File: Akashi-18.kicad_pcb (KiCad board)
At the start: 2 copper layers, 54.6 x 91.4 mm, 13 parts, among them Q1 DTC143Z, Q2 DTC143Z, Q3 DTC143Z, SW1 B3FS, SW2 B3FS, SW3 B3FS, U1 Pico

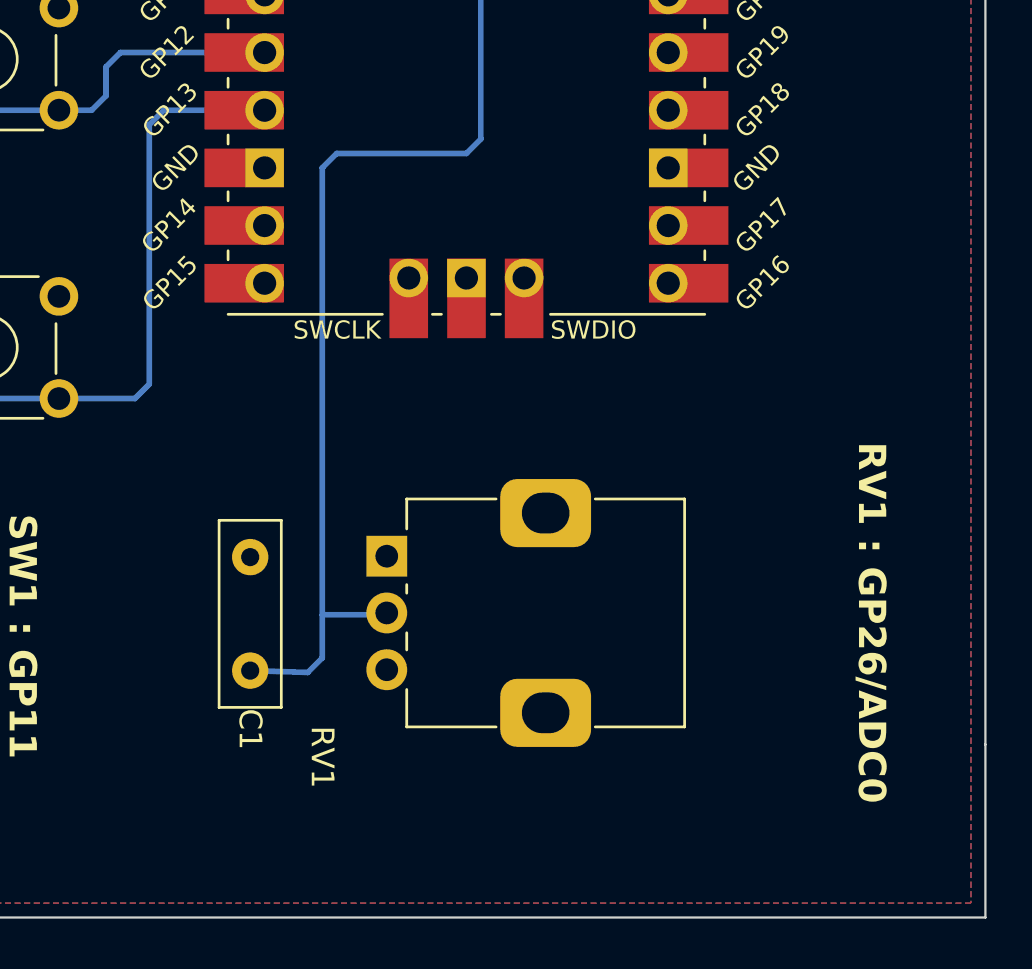
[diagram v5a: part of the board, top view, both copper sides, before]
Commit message: Correct the parts list and refine the PCB layout.
Volume -> A-curve.
RasPi Pico -> wo Header.
Connector -> Conthrough.

PCB layout has been refined for the better visibility of the
RV1 comment.
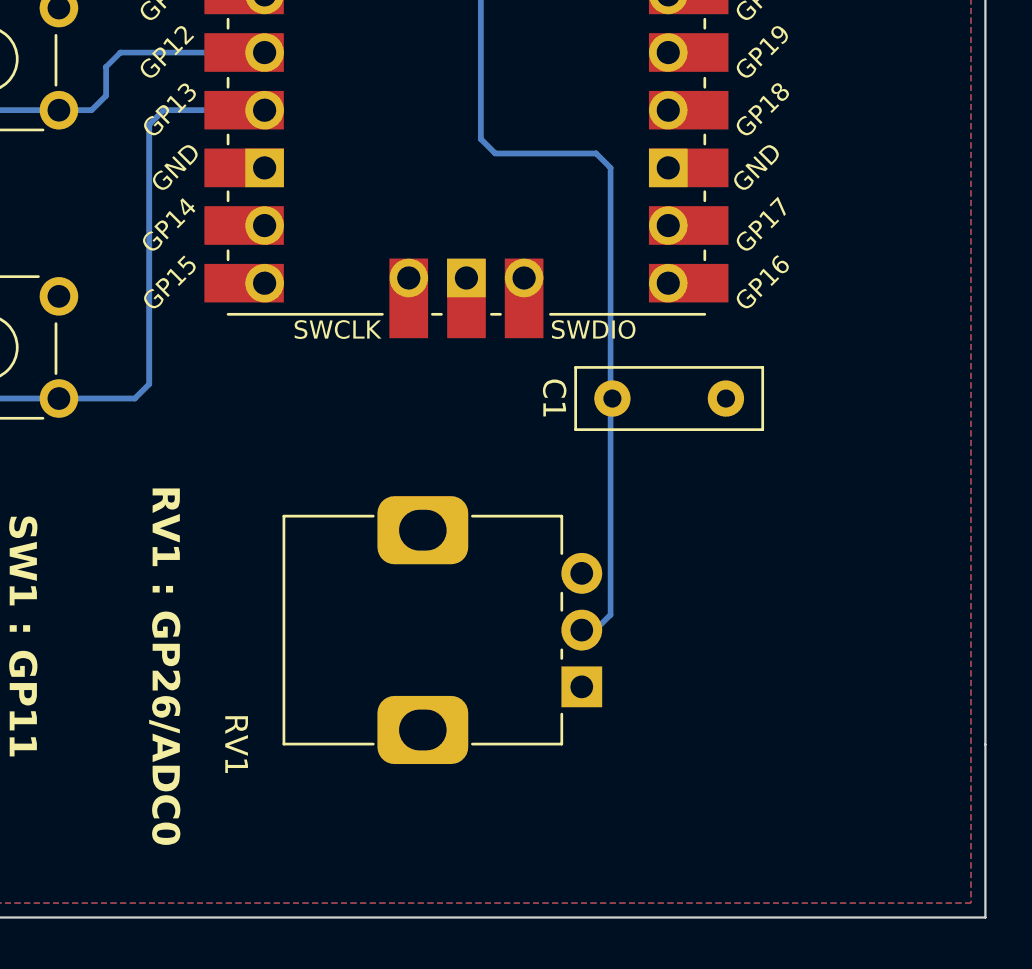
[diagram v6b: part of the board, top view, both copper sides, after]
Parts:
- RV1: value RK09D117000B -> RK09D117000C
- moved C1 20.0 mm to (127.1, 119.4), turned to 0 degrees
- moved RV1 10.3 mm to (125.7, 132.1), turned to 180 degrees
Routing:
- net Net-(U1-GPIO26_ADC0): track 62.3 -> 54.4 mm
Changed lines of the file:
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@@
   )
   (footprint "Capacitor_THT:C_Disc_D8.0mm_W2.5mm_P5.00mm" (layer "F.Cu")
-    (at 111.125 131.365 90)
+    (at 127.08 119.38)
     (descr "C, Disc series, Radial, pin pitch=5.00mm, , diameter*width=8*2.5mm^2, Capacitor, http://cdn-reichelt.de/documents/datenblatt/B300/DS_KERKO_TC.pdf")
     (tags "C Disc series Radial pin pitch 5.00mm  diameter 8mm width 2.5mm Capacitor")
@@
     (property "ki_keywords" "cap capacitor")
     (attr through_hole)
-    (fp_text reference "C1" (at -2.58 0 270 unlocked) (layer "F.SilkS")
-        (effects (font (size 1 1) (thickness 0.15)))
-    )
-    (fp_text value "0.1u" (at 2.5 2.5 90) (layer "F.Fab")
-        (effects (font (size 1 1) (thickness 0.15)))
-    )
-    (fp_text user "${REFERENCE}" (at 2.5 0 90) (layer "F.Fab")
+    (fp_text reference "C1" (at -2.58 0 -90 unlocked) (layer "F.SilkS")
+        (effects (font (size 1 1) (thickness 0.15)))
+    )
+    (fp_text value "0.1u" (at 2.5 2.5) (layer "F.Fab")
+        (effects (font (size 1 1) (thickness 0.15)))
+    )
+    (fp_text user "${REFERENCE}" (at 2.5 0) (layer "F.Fab")
         (effects (font (size 1 1) (thickness 0.15)))
     )
@@
     (fp_line (start 6.5 1.25) (end 6.5 -1.25)
       (stroke (width 0.1) (type solid)) (layer "F.Fab"))
-    (pad "1" thru_hole circle (at 0 0 90) (size 1.6 1.6) (drill 0.8) (layers "*.Cu" "*.Mask")
+    (pad "1" thru_hole circle (at 0 0) (size 1.6 1.6) (drill 0.8) (layers "*.Cu" "*.Mask")
       (net 12 "Net-(U1-GPIO26_ADC0)") (pintype "passive"))
-    (pad "2" thru_hole circle (at 5 0 90) (size 1.6 1.6) (drill 0.8) (layers "*.Cu" "*.Mask")
+    (pad "2" thru_hole circle (at 5 0) (size 1.6 1.6) (drill 0.8) (layers "*.Cu" "*.Mask")
       (net 5 "GND") (pintype "passive"))
     (model "${KICAD6_3DMODEL_DIR}/Capacitor_THT.3dshapes/C_Disc_D8.0mm_W2.5mm_P5.00mm.wrl"
@@
   )
   (footprint "Potentiometer_THT:Potentiometer_Alps_RK09K_Single_Vertical" (layer "F.Cu")
-    (at 117.14 126.325)
+    (at 125.73 132.08 180)
     (descr "113004U 1130A6S 11300DR 1130A8G 1130081 1130A5R 1130AP5 1130AST  D1130C3W D1130C1B D1130C3C D1130C2P Potentiometer, vertical, Alps RK09K Single, https://tech.alpsalpine.com/prod/e/pdf/potentiometer/rotarypotentiometers/rk09k/rk09k.pdf")
     (tags "Potentiometer vertical Alps RK09K RK09D Single Snapin")
@@
     (property "ki_keywords" "resistor variable")
     (attr through_hole)
-    (fp_text reference "RV1" (at -2.84 8.85 -90 unlocked) (layer "F.SilkS")
-        (effects (font (size 1 1) (thickness 0.15)))
-    )
-    (fp_text value "RK09D117000B" (at 6.05 10.15) (layer "F.Fab")
+    (fp_text reference "RV1" (at 15.24 -2.54 270 unlocked) (layer "F.SilkS")
+        (effects (font (size 1 1) (thickness 0.15)))
+    )
+    (fp_text value "RK09D117000C" (at 6.05 10.15) (layer "F.Fab")
         (effects (font (size 1 1) (thickness 0.15)))
     )
@@
     (fp_circle (center 7.5 2.5) (end 10.5 2.5)
       (stroke (width 0.1) (type solid)) (fill none) (layer "F.Fab"))
-    (pad "1" thru_hole rect (at 0 0) (size 1.8 1.8) (drill 1) (layers "*.Cu" "*.Mask")
+    (pad "1" thru_hole rect (at 0 0 180) (size 1.8 1.8) (drill 1) (layers "*.Cu" "*.Mask")
       (net 5 "GND") (pinfunction "1") (pintype "passive"))
-    (pad "2" thru_hole circle (at 0 2.5) (size 1.8 1.8) (drill 1) (layers "*.Cu" "*.Mask")
+    (pad "2" thru_hole circle (at 0 2.5 180) (size 1.8 1.8) (drill 1) (layers "*.Cu" "*.Mask")
       (net 12 "Net-(U1-GPIO26_ADC0)") (pinfunction "2") (pintype "passive"))
-    (pad "3" thru_hole circle (at 0 5) (size 1.8 1.8) (drill 1) (layers "*.Cu" "*.Mask")
+    (pad "3" thru_hole circle (at 0 5 180) (size 1.8 1.8) (drill 1) (layers "*.Cu" "*.Mask")
       (net 42 "/3V3") (pinfunction "3") (pintype "passive"))
-    (pad "MP" thru_hole roundrect (at 7 -1.9) (size 4 3) (drill oval 2.1 1.8) (layers "*.Cu" "*.Mask") (roundrect_rratio 0.25)
+    (pad "MP" thru_hole roundrect (at 7 -1.9 180) (size 4 3) (drill oval 2.1 1.8) (layers "*.Cu" "*.Mask") (roundrect_rratio 0.25)
       (net 5 "GND") (pinfunction "MountPin") (pintype "passive"))
-    (pad "MP" thru_hole roundrect (at 7 6.9) (size 4 3) (drill oval 2.1 1.8) (layers "*.Cu" "*.Mask") (roundrect_rratio 0.25)
+    (pad "MP" thru_hole roundrect (at 7 6.9 180) (size 4 3) (drill oval 2.1 1.8) (layers "*.Cu" "*.Mask") (roundrect_rratio 0.25)
       (net 5 "GND") (pinfunction "MountPin") (pintype "passive"))
     (model "${KICAD6_3DMODEL_DIR}/Potentiometer_THT.3dshapes/Potentiometer_Alps_RK09K_Single_Vertical.wrl"
@@
     (effects (font (size 1.5 1.5) (thickness 0.3) bold) (justify left bottom mirror))
   )
-  (gr_text "RV1 : GP26/ADC0" (at 137.795 121.285 270) (layer "F.SilkS")
+  (gr_text "RV1 : GP26/ADC0" (at 106.68 123.19 270) (layer "F.SilkS")
     (effects (font (size 1.2 1.2) (thickness 0.2) bold) (justify left bottom))
   )
@@
   (segment (start 129.54 88.9) (end 121.92 88.9) (width 0.25) (layer "F.Cu") (net 12))
   (via (at 121.92 88.9) (size 0.8) (drill 0.4) (layers "F.Cu" "B.Cu") (net 12))
+  (segment (start 126.365 108.585) (end 127 109.22) (width 0.25) (layer "B.Cu") (net 12))
+  (segment (start 125.73 129.58) (end 126.325 129.58) (width 0.25) (layer "B.Cu") (net 12))
+  (segment (start 126.325 129.58) (end 127 128.905) (width 0.25) (layer "B.Cu") (net 12))
+  (segment (start 127 109.22) (end 127 128.905) (width 0.25) (layer "B.Cu") (net 12))
+  (segment (start 121.92 108.585) (end 126.365 108.585) (width 0.25) (layer "B.Cu") (net 12))
+  (segment (start 121.285 89.535) (end 121.285 107.95) (width 0.25) (layer "B.Cu") (net 12))
+  (segment (start 121.285 107.95) (end 121.92 108.585) (width 0.25) (layer "B.Cu") (net 12))
   (segment (start 121.92 88.9) (end 121.285 89.535) (width 0.25) (layer "B.Cu") (net 12))
-  (segment (start 114.935 108.585) (end 114.3 109.22) (width 0.25) (layer "B.Cu") (net 12))
-  (segment (start 117.14 128.905) (end 114.3 128.905) (width 0.25) (layer "B.Cu") (net 12))
-  (segment (start 121.285 107.95) (end 120.65 108.585) (width 0.25) (layer "B.Cu") (net 12))
-  (segment (start 114.3 130.81) (end 113.665 131.445) (width 0.25) (layer "B.Cu") (net 12))
-  (segment (start 121.285 89.535) (end 121.285 107.95) (width 0.25) (layer "B.Cu") (net 12))
-  (segment (start 113.665 131.445) (end 111.125 131.365) (width 0.25) (layer "B.Cu") (net 12))
-  (segment (start 114.3 109.22) (end 114.3 130.81) (width 0.25) (layer "B.Cu") (net 12))
-  (segment (start 120.65 108.585) (end 114.935 108.585) (width 0.25) (layer "B.Cu") (net 12))
   (segment (start 106.68 118.745) (end 106.68 107.315) (width 0.25) (layer "B.Cu") (net 13))
   (segment (start 96.2 119.38) (end 106.045 119.38) (width 0.25) (layer "B.Cu") (net 13))
